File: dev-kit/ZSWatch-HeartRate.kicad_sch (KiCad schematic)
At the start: 50 parts, among them IC101 LIS2DS12, IC102 MCP73832-2-OT, IC103 MAX32664, IC104 TPS61240, IC105 MAX86141, IC106 MIC5365-1.8, J101 SPI, J102 GPIO, J103 UART, J104 I2C, M101 BM15C, Q101 BSS138, SW101 BTN1, SW102 RESET, X102 CHARGE, X103 BATTERY, X104 DEBUG, Y101 32kHz

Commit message: doc: Add missing part informations
Signed-off-by: Daniel Kampert <DanielKampert@kampis-elektroecke.de>
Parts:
- C104, C111, C112, C117: manf (none) -> KYOCERA AVX; manf# (none) -> 04023D105KAT2A; mouser# (none) -> 581-04023D105KAT2A
- IC101: manf (none) -> STMicroelectronics; manf# (none) -> LIS2DS12; mouser# (none) -> 511-LIS2DS12
- L101: manf (none) -> ABRACON; manf# (none) -> ASMCI-0603-1R0M-T; mouser# (none) -> 815-ASMCI-0603-1R0MT
- R109: manf (none) -> Vishay; manf# (none) -> CRCW08050000Z0EBC; mouser# (none) -> 71-CRCW08050000Z0EBC
- X102: manf (none) -> GCT; manf# (none) -> USB4105-GF-A-120; mouser# (none) -> 640-USB4105-GF-A-120
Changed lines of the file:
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@@
 			)
 		)
-		(property "Datasheet" "https://www.mouser.de/datasheet/2/447/YAGEO_PYu_RC_Group_51_RoHS_L_12-3313492.pdf"
+		(property "Datasheet" "https://www.vishay.com/doc?28773"
 			(at 128.27 232.41 0)
 			(effects
@@
 			)
 		)
-		(property "manf" ""
+		(property "manf" "Vishay"
 			(at 128.27 232.41 0)
 			(effects
@@
 			)
 		)
-		(property "manf#" ""
+		(property "manf#" "CRCW08050000Z0EBC"
 			(at 128.27 232.41 0)
 			(effects
@@
 			)
 		)
-		(property "mouser#" ""
+		(property "mouser#" "71-CRCW08050000Z0EBC"
 			(at 128.27 232.41 0)
 			(effects
@@
 			)
 		)
-		(property "Datasheet" "~"
+		(property "Datasheet" "https://www.mouser.de/datasheet/2/40/cx5r_KGM-3223198.pdf"
 			(at 176.53 105.41 0)
 			(effects
@@
 			)
 		)
-		(property "manf" ""
+		(property "manf" "KYOCERA AVX"
 			(at 176.53 105.41 0)
 			(effects
@@
 			)
 		)
-		(property "manf#" ""
+		(property "manf#" "04023D105KAT2A"
 			(at 176.53 105.41 0)
 			(effects
@@
 			)
 		)
-		(property "mouser#" ""
+		(property "mouser#" "581-04023D105KAT2A"
 			(at 176.53 105.41 0)
 			(effects
@@
 			)
 		)
-		(property "Datasheet" "~"
+		(property "Datasheet" "https://www.mouser.de/datasheet/2/40/cx5r_KGM-3223198.pdf"
 			(at 198.12 105.41 0)
 			(effects
@@
 			)
 		)
-		(property "manf" ""
+		(property "manf" "KYOCERA AVX"
 			(at 198.12 105.41 0)
 			(effects
@@
 			)
 		)
-		(property "manf#" ""
+		(property "manf#" "04023D105KAT2A"
 			(at 198.12 105.41 0)
 			(effects
@@
 			)
 		)
-		(property "mouser#" ""
+		(property "mouser#" "581-04023D105KAT2A"
 			(at 198.12 105.41 0)
 			(effects
@@
 			)
 		)
-		(property "Datasheet" "~"
+		(property "Datasheet" "https://www.we-online.com/components/products/datasheet/430182095816.pdf"
 			(at 139.7 224.79 0)
 			(effects
@@
 			)
 		)
-		(property "Datasheet" "~"
+		(property "Datasheet" "https://www.mouser.de/datasheet/2/40/cx5r_KGM-3223198.pdf"
 			(at 187.96 105.41 0)
 			(effects
@@
 			)
 		)
-		(property "manf" ""
+		(property "manf" "KYOCERA AVX"
 			(at 187.96 105.41 0)
 			(effects
@@
 			)
 		)
-		(property "manf#" ""
+		(property "manf#" "04023D105KAT2A"
 			(at 187.96 105.41 0)
 			(effects
@@
 			)
 		)
-		(property "mouser#" ""
+		(property "mouser#" "581-04023D105KAT2A"
 			(at 187.96 105.41 0)
 			(effects
@@
 			)
 		)
-		(property "manf" ""
+		(property "manf" "GCT"
 			(at 185.42 48.26 0)
 			(effects
@@
 			)
 		)
-		(property "manf#" ""
+		(property "manf#" "USB4105-GF-A-120"
 			(at 185.42 48.26 0)
 			(effects
@@
 			)
 		)
-		(property "mouser#" ""
+		(property "mouser#" "640-USB4105-GF-A-120"
 			(at 185.42 48.26 0)
 			(effects
@@
 			)
 		)
-		(property "Datasheet" "~"
+		(property "Datasheet" "https://www.mouser.de/datasheet/2/40/cx5r_KGM-3223198.pdf"
 			(at 285.75 96.52 0)
 			(effects
@@
 			)
 		)
-		(property "manf" ""
+		(property "manf" "KYOCERA AVX"
 			(at 285.75 96.52 0)
 			(effects
@@
 			)
 		)
-		(property "manf#" ""
+		(property "manf#" "04023D105KAT2A"
 			(at 285.75 96.52 0)
 			(effects
@@
 			)
 		)
-		(property "mouser#" ""
+		(property "mouser#" "581-04023D105KAT2A"
 			(at 285.75 96.52 0)
 			(effects
@@
 			)
 		)
-		(property "Datasheet" "https://product.tdk.com/system/files/dam/doc/product/inductor/inductor/smd/catalog/inductor_commercial_decoupling_mlz1005_en.pdf?ref_disty=mouser"
+		(property "Datasheet" "https://www.mouser.de/datasheet/2/3/ASMCI_0603-3318216.pdf"
 			(at 379.73 20.32 0)
 			(effects
@@
 			)
 		)
+		(property "manf" "ABRACON"
+			(at 379.73 20.32 90)
+			(effects
+				(font
+					(size 1.27 1.27)
+				)
+				(hide yes)
+			)
+		)
+		(property "manf#" "ASMCI-0603-1R0M-T"
+			(at 379.73 20.32 90)
+			(effects
+				(font
+					(size 1.27 1.27)
+				)
+				(hide yes)
+			)
+		)
+		(property "mouser#" "815-ASMCI-0603-1R0MT"
+			(at 379.73 20.32 90)
+			(effects
+				(font
+					(size 1.27 1.27)
+				)
+				(hide yes)
+			)
+		)
 		(pin "2"
 		)
@@
 			)
 		)
-		(property "Datasheet" ""
+		(property "Datasheet" "https://www.mouser.de/datasheet/2/915/BM15C_2bProduct_2bSpecifications-3555318.pdf"
 			(at 63.754 171.196 0)
 			(effects
@@
 			)
 		)
-		(property "Datasheet" "~"
+		(property "Datasheet" "https://www.we-online.com/components/products/datasheet/430182095816.pdf"
 			(at 35.56 185.42 0)
 			(effects
@@
 			)
 		)
-		(property "manf" ""
+		(property "manf" "STMicroelectronics"
 			(at 297.18 213.36 0)
 			(effects
@@
 			)
 		)
-		(property "manf#" ""
+		(property "manf#" "LIS2DS12"
 			(at 297.18 213.36 0)
 			(effects
@@
 			)
 		)
-		(property "mouser#" ""
+		(property "mouser#" "511-LIS2DS12"
 			(at 297.18 213.36 0)
 			(effects

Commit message: Issue #4
Signed-off-by: Daniel Kampert <DanielKampert@kampis-elektroecke.de>
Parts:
- added D101: D_Photo, Vishay:VEMD5080X01, symbol Device:D_Photo
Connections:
- net GND: no longer D102.2 (A), IC105.C5 (PD_GND), IC105.D4 (NC)
- new net: D101.1 (K), IC105.D4 (NC)
- new net PD_GND: D101.2 (A), D102.2 (A), IC105.C5 (PD_GND)
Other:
- note removed: "TODO: Can we use GPIO1 or 2 to Enable / Disable VLED?"

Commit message: Rework heartrate sensor
- Issue #7
- Issue #6
- Issue #5
- Issue #4

Signed-off-by: Daniel Kampert <DanielKampert@kampis-elektroecke.de>
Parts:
- removed D104: IR, Diode_SMD:D_0603_1608Metric, symbol Device:LED
- removed D105: GREEN, Diode_SMD:D_0603_1608Metric, symbol Device:LED
- removed D106: RED, Diode_SMD:D_0603_1608Metric, symbol Device:LED
- removed J102: GPIO, Connector_PinHeader_2.54mm:PinHeader_1x07_P2.54mm_Vertical, symbol Connector_Generic:Conn_01x07
- removed J103: UART, Connector_PinHeader_2.54mm:PinHeader_1x03_P2.54mm_Vertical, symbol Connector_Generic:Conn_01x03
- added C118: ~, Capacitor_SMD:C_0402_1005Metric, symbol Device:C_Small
- added LED101: SFH 7016, Osram:SFH7016, symbol Osram:SFH7016
- added R110: ~, Resistor_SMD:R_0402_1005Metric, symbol Device:R
- D101, D102: footprint Vishay:VEMD5080X01 -> Vishay:VEMD8080; manf# VEMD5080X01 -> VEMD8080; mouser# 78-VEMD5080X01 -> 78-VEMD8080
- X104: manf Samtec -> Wurth Elektronik; manf# SHF-105-01-L-D-TH-TR -> 623310235521; mouser# 200-SHF-105-01-L-D-TH-TR -> 710-623310235521
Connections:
- net CHARGE: now also M101.K5 (P2.10); no longer M101.J6 (P2.07)
- net GND: now also C118.2, R110.2
- net PD_GND: now also C118.1, R110.1
- net SCL: now also M101.G8 (P1.08); no longer M101.K6 (P2.08)
- net SDA: now also M101.G9 (P1.07/AIN3); no longer M101.K5 (P2.10)
- net V_{LED}: now also LED101.2 (A), LED101.5 (A)
- net at R109.1: now also M101.K4 (P0.01); no longer M101.K7 (P2.06)
- net at IC105.B1 (LED3_DRV): now also LED101.4 (K)
- net at IC101.4 (SDA/SDI/SDO), IC103.20 (MOSI_{SENSOR}), IC105.A4 (MOSI): now also J101.4 (Pin_4); no longer J101.2 (Pin_2)
- net at IC101.1 (SCL/SCLK), IC103.19 (SCLK_{SENSOR}), IC105.A2 (SCLK): now also J101.2 (Pin_2); no longer J101.4 (Pin_4)
- net at IC101.2 (CS), IC103.2 (CS_{ACC}): now also J101.6 (Pin_6); no longer J101.5 (Pin_5)
- net at IC103.18 (CS_{PPG}), IC105.A5 (~{CSB}): now also J101.5 (Pin_5); no longer J101.6 (Pin_6)
- net at IC105.C1 (LED2_DRV): now also LED101.1 (K)
- net at IC105.D1 (LED1_DRV): now also LED101.3 (K)
- net at M101.K2 (P0.02): now also Q101.1 (G)
- net at M101.K8 (P2.05): no longer Q101.1 (G)
- net TxD: no longer names the net of M101.E8 (P1.03/NFC)
- no-connect marks 26 -> 34
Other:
- note removed: "557 nm"
- note removed: "660 nm"
- note removed: "880 nm"
- moved on the sheet: D107, Q101, R105, R109

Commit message: Issue #8
Signed-off-by: Daniel Kampert <DanielKampert@kampis-elektroecke.de>
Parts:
- D101, D102: footprint Vishay:VEMD8080 -> Vishay:VEMD808x; manf# VEMD8080 -> VEMD8082; mouser# 78-VEMD8080 -> 78-VEMD8082
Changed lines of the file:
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@@
 			)
 		)
-		(property "Footprint" "Vishay:VEMD8080"
+		(property "Footprint" "Vishay:VEMD808x"
 			(at 318.77 132.08 0)
 			(effects
@@
 			)
 		)
-		(property "Datasheet" "https://www.vishay.com/doc?84565"
+		(property "Datasheet" "https://www.vishay.com/docs/80381/vemd8082.pdf"
 			(at 318.77 132.08 0)
 			(effects
@@
 			)
 		)
-		(property "manf#" "VEMD8080"
+		(property "manf#" "VEMD8082"
 			(at 320.04 132.08 0)
 			(effects
@@
 			)
 		)
-		(property "mouser#" "78-VEMD8080"
+		(property "mouser#" "78-VEMD8082"
 			(at 320.04 132.08 0)
 			(effects
@@
 			)
 		)
-		(property "Footprint" "Vishay:VEMD8080"
+		(property "Footprint" "Vishay:VEMD808x"
 			(at 318.77 128.27 0)
 			(effects
@@
 			)
 		)
-		(property "Datasheet" "https://www.vishay.com/doc?84565"
+		(property "Datasheet" "https://www.vishay.com/docs/80381/vemd8082.pdf"
 			(at 318.77 128.27 0)
 			(effects
@@
 			)
 		)
-		(property "manf#" "VEMD8080"
+		(property "manf#" "VEMD8082"
 			(at 320.04 128.27 0)
 			(effects
@@
 			)
 		)
-		(property "mouser#" "78-VEMD8080"
+		(property "mouser#" "78-VEMD8082"
 			(at 320.04 128.27 0)
 			(effects

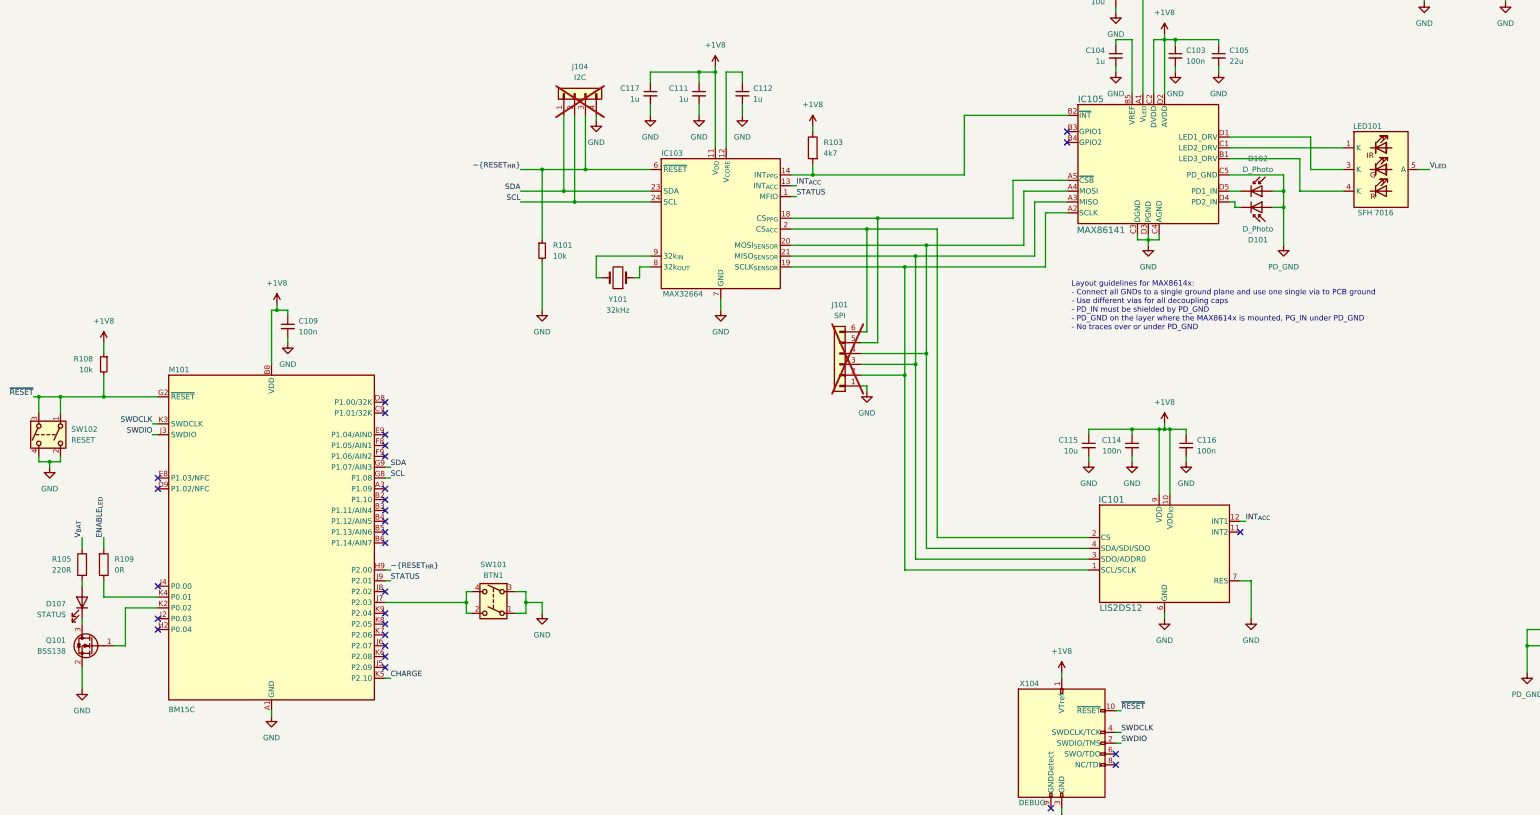
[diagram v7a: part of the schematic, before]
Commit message: Feature: Issue #16
- Add MFIO to SPI header

Signed-off-by: Daniel Kampert <DanielKampert@kampis-elektroecke.de>
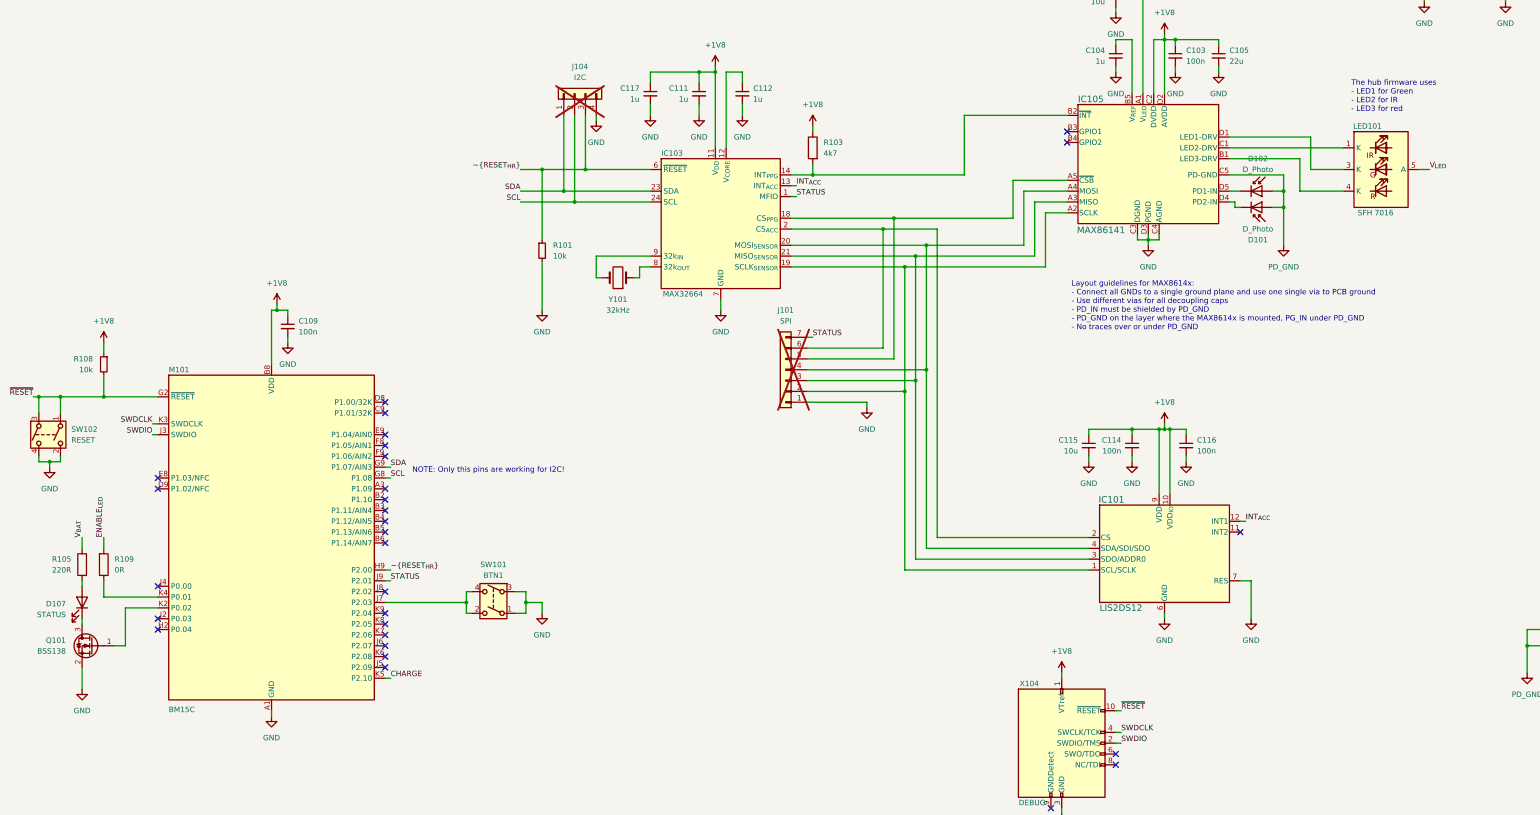
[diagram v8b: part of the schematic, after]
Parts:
- J101: footprint Connector_PinHeader_2.54mm:PinHeader_1x06_P2.54mm_Vertical -> Connector_PinHeader_2.54mm:PinHeader_1x07_P2.54mm_Vertical; symbol Connector_Generic:Conn_01x06 -> Connector_Generic:Conn_01x07
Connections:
- net STATUS: now also J101.7 (Pin_7)
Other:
- note added: "NOTE: Only this pins are working for I2C!"
- note added: "The hub firmware uses - LED1 for Green - LED2 for IR - LED3 for red"
